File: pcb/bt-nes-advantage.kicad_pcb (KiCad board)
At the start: 2 copper layers, 78 x 35 mm, 20 parts, among them J1 USB_C_Receptacle_PowerOnly_6P, J2 Screw_Terminal_01x02, J3 Conn_01x08, U1 ESP32-C3_SUPERMINI_TH, U2 HW775

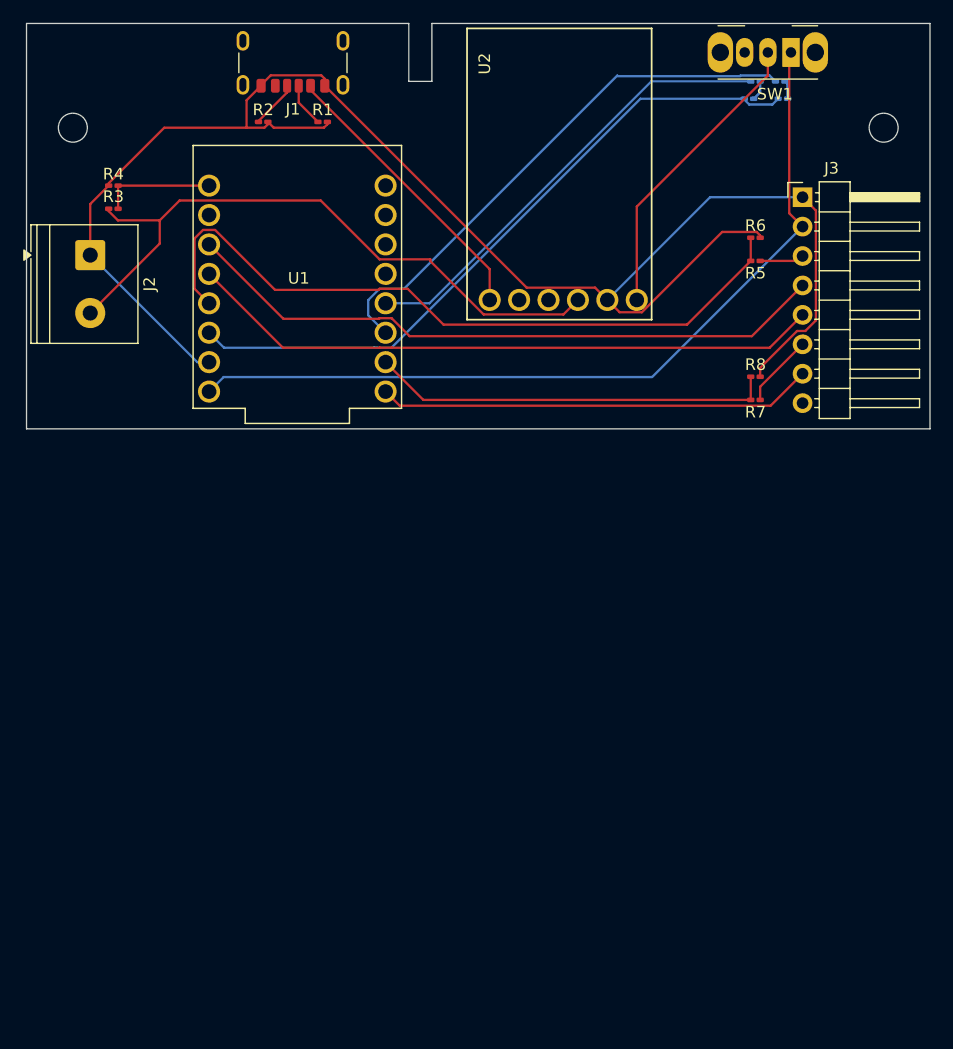
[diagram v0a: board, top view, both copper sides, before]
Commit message: New PCB revision. Updated firmware logic.
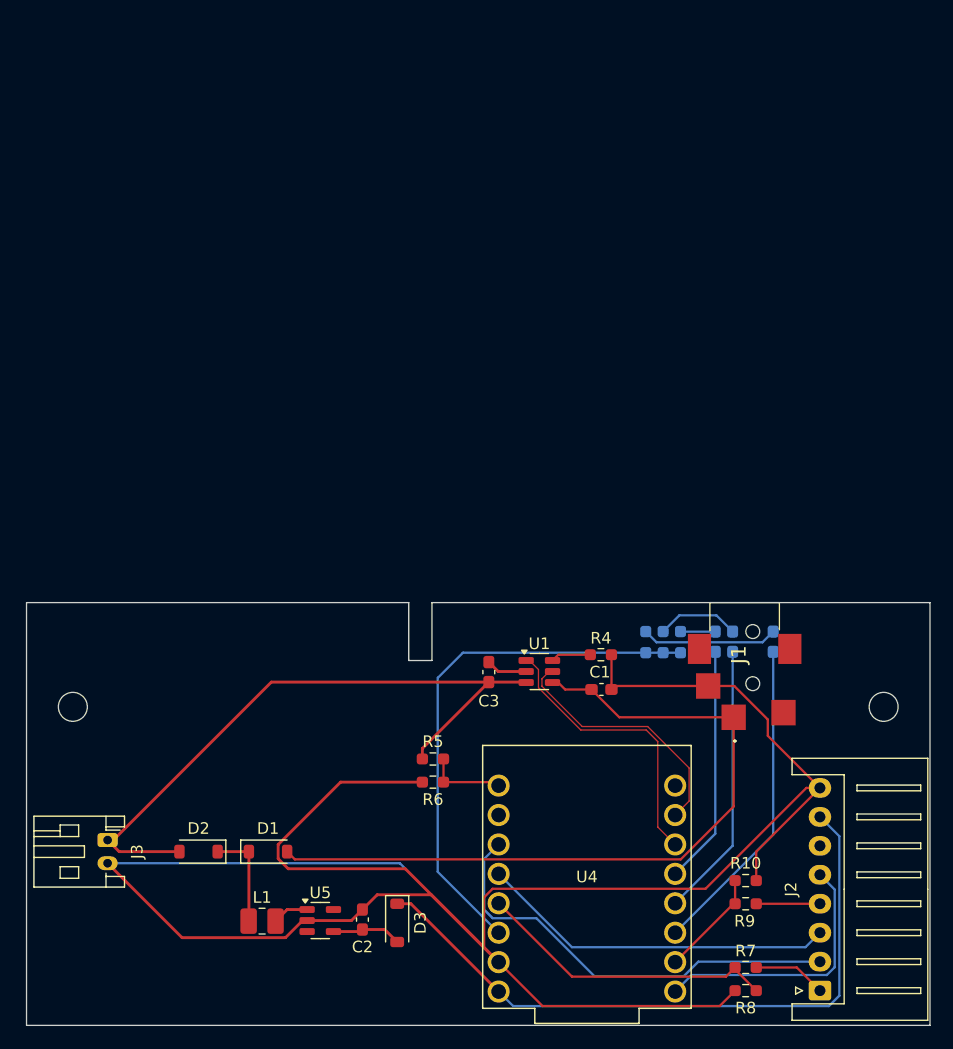
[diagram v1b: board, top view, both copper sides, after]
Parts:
- removed the REF** at (104.0, 59.0)
- removed the REF** at (174.0, 59.0)
- removed SW1: ~, Button_Switch_THT:SW_Slide_SPDT_Angled_CK_OS102011MA1Q
- removed U2: HW775, bt-nes-advantage:Charger2A
- added C1: 10µF, Capacitor_SMD:C_0603_1608Metric_Pad1.08x0.95mm_HandSolder, F.Cu at (149.6, 107.5)
- added C2: 22µF, Capacitor_SMD:C_0603_1608Metric_Pad1.08x0.95mm_HandSolder, F.Cu at (129.0, 127.4)
- added C3: 10µF, Capacitor_SMD:C_0603_1608Metric_Pad1.08x0.95mm_HandSolder, F.Cu at (139.9, 106.0)
- added D3: 1N5817W, Diode_SMD:D_SOD-123, F.Cu at (132.0, 127.7)
- added D4: LED, LED_SMD:LED_0603_1608Metric_Pad1.05x0.95mm_HandSolder, B.Cu at (164.5, 103.4)
- added D5: LED, LED_SMD:LED_0603_1608Metric_Pad1.05x0.95mm_HandSolder, B.Cu at (161.0, 103.4)
- added D6: LED, LED_SMD:LED_0603_1608Metric_Pad1.05x0.95mm_HandSolder, B.Cu at (159.5, 103.4)
- added L1: 2.2µH, Inductor_SMD:L_1008_2520Metric_Pad1.43x2.20mm_HandSolder, F.Cu at (120.3, 127.5)
- added REF**: MountingHole_2.5mm, MountingHole:MountingHole_2.5mm, F.Cu at (174.0, 109.0)
- added REF**: MountingHole_2.5mm, MountingHole:MountingHole_2.5mm, F.Cu at (104.0, 109.0)
- added U4: ESP32-C3_SUPERMINI_TH, My_Library:MODULE_ESP32-C3_SUPERMINI, F.Cu at (148.4, 123.7)
- added U5: TPS613222ADBV, Package_TO_SOT_SMD:SOT-23-5, F.Cu at (125.4, 127.5)
- D1, D2: value LED -> 1N5817W; footprint LED_SMD:LED_0201_0603Metric_Pad0.64x0.40mm_HandSolder -> Diode_SMD:D_SOD-123; moved to F.Cu
- J1: value USB_C_Receptacle_PowerOnly_6P -> PJ-043-SMT-TR; footprint Connector_USB:USB_C_Receptacle_GCT_USB4125-xx-x-0190_6P_TopMnt_Horizontal -> My_Library:PJ043SMTTR
- J2: value Screw_Terminal_01x02 -> Conn_01x08_Socket; footprint TerminalBlock_Phoenix:TerminalBlock_Phoenix_PT-1,5-2-5.0-H_1x02_P5.00mm_Horizontal -> Connector_JST:JST_XH_S8B-XH-A_1x08_P2.50mm_Horizontal
- J3: value Conn_01x08 -> 3.7V Lithium Battery; footprint Connector_PinHeader_2.54mm:PinHeader_1x08_P2.54mm_Horizontal -> Connector_JST:JST_PH_S2B-PH-K_1x02_P2.00mm_Horizontal
- R1, R2: value 5.1K -> 200; footprint Resistor_SMD:R_0201_0603Metric_Pad0.64x0.40mm_HandSolder -> Resistor_SMD:R_0603_1608Metric_Pad0.98x0.95mm_HandSolder; moved to B.Cu
- R10, R9: value 200 -> 1K; footprint Resistor_SMD:R_0201_0603Metric_Pad0.64x0.40mm_HandSolder -> Resistor_SMD:R_0603_1608Metric_Pad0.98x0.95mm_HandSolder; moved to F.Cu
- R3: value 100K -> 200; footprint Resistor_SMD:R_0201_0603Metric_Pad0.64x0.40mm_HandSolder -> Resistor_SMD:R_0603_1608Metric_Pad0.98x0.95mm_HandSolder; moved to B.Cu
- R4: value 100K -> 2K; footprint Resistor_SMD:R_0201_0603Metric_Pad0.64x0.40mm_HandSolder -> Resistor_SMD:R_0603_1608Metric_Pad0.98x0.95mm_HandSolder
- R5: value 1K -> 100K; footprint Resistor_SMD:R_0201_0603Metric_Pad0.64x0.40mm_HandSolder -> Resistor_SMD:R_0603_1608Metric_Pad0.98x0.95mm_HandSolder
- R6: value 2K -> 100K; footprint Resistor_SMD:R_0201_0603Metric_Pad0.64x0.40mm_HandSolder -> Resistor_SMD:R_0603_1608Metric_Pad0.98x0.95mm_HandSolder
- R7: footprint Resistor_SMD:R_0201_0603Metric_Pad0.64x0.40mm_HandSolder -> Resistor_SMD:R_0603_1608Metric_Pad0.98x0.95mm_HandSolder
- R8: value 2K -> 1K; footprint Resistor_SMD:R_0201_0603Metric_Pad0.64x0.40mm_HandSolder -> Resistor_SMD:R_0603_1608Metric_Pad0.98x0.95mm_HandSolder
- U1: value ESP32-C3_SUPERMINI_TH -> TP4057; footprint bt-nes-advantage:MODULE_ESP32-C3_SUPERMINI -> Package_TO_SOT_SMD:TSOT-23-6
- moved J2 89.4 mm to (168.5, 133.5), turned to 90 degrees
- moved D2 83.3 mm to (114.8, 121.5), turned to 180 degrees
- moved J3 81.7 mm to (107.0, 120.5), turned to -90 degrees
- moved D1 78.7 mm to (120.8, 121.5)
- moved R9 69.5 mm to (162.1, 126.0), turned to 0 degrees
- moved R10 67.6 mm to (162.1, 124.0)
- moved J1 65.8 mm to (162.0, 105.2), turned to -90 degrees
- moved R3 61.6 mm to (156.5, 103.4), turned to -90 degrees
- moved R4 58.4 mm to (149.6, 104.5), turned to 0 degrees
- moved R2 56.7 mm to (155.0, 103.4), turned to -90 degrees
- moved R6 54.6 mm to (135.1, 115.5)
- moved R8 53.0 mm to (162.1, 133.5)
- moved R1 52.9 mm to (153.5, 103.4), turned to -90 degrees
- moved R5 51.2 mm to (135.1, 113.5)
- moved R7 49.0 mm to (162.1, 131.5), turned to 0 degrees
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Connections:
- D1 pad 1: /LED 1 -> Net-(D1-K)
- D1 pad 2: Net-(D1-A) -> VBUS_5V
- D2 pad 1: /LED 2 -> Net-(D1-K)
- D2 pad 2: Net-(D2-A) -> VBAT
- J2 pad 1: GND -> DATA_0_5V
- J2 pad 2: +BATT -> LATCH
- J3 pad 1: GND -> VBAT
- J3 pad 2: +5V -> GND
- R1 pad 1: Net-(J1-CC1) -> Net-(D4-A)
- R1 pad 2: GND -> VDD_3V
- R10 pad 1: Net-(D2-A) -> GND
- R10 pad 2: +3.3V -> DATA_1
- R2 pad 1: Net-(J1-CC2) -> Net-(D5-A)
- R2 pad 2: GND -> VDD_3V
- R3 pad 1: +BATT -> Net-(D6-A)
- R3 pad 2: /BATT READ -> VDD_3V
- R4 pad 1: /BATT READ -> Net-(U1-PROG)
- R5 pad 1: /DATA 0 5V -> BATT_READ
- R5 pad 2: /DATA 0 -> VBAT
- R6 pad 1: /DATA 0 -> GND
- R6 pad 2: GND -> BATT_READ
- R7 pad 1: /DATA 1 5V -> DATA_0
- R7 pad 2: /DATA 1 -> DATA_0_5V
- R8 pad 1: /DATA 1 -> GND
- R8 pad 2: GND -> DATA_0
- R9 pad 1: Net-(D1-A) -> DATA_1
- R9 pad 2: +3.3V -> DATA_1_5V
- U1 pad 1: unconnected-(U1-GPIO1-Pad1) -> BATT_CHRG
- U1 pad 2: /LATCH -> GND
- U1 pad 3: /CLOCK 0 -> VBAT
- U1 pad 4: /DATA 0 -> VBUS_5V
- U1 pad 5: /CLOCK 1 -> BATT_STDBY
- U1 pad 6: /DATA 1 -> Net-(U1-PROG)
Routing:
- net GND: track 141.3 -> 217.3 mm
- net +5V: track 72.7 -> 0.00 mm
- net VBUS_5V: track 0.00 -> 65.3 mm
- net /DATA 0: track 62.2 -> 0.00 mm
- net +3.3V: track 59.0 -> 0.00 mm
- net VDD_5V: track 0.00 -> 58.3 mm
- net VBAT: track 0.00 -> 57.4 mm
- net +BATT: track 56.9 -> 0.00 mm
- net /LATCH: track 56.4 -> 0.00 mm
- net /CLOCK 0: track 55.1 -> 0.00 mm
- net /LED 2: track 46.9 -> 0.00 mm
- net VDD_3V: track 0.00 -> 46.0 mm
- net /LED 1: track 39.5 -> 0.00 mm
- net LATCH: track 0.00 -> 38.1 mm
- net /CLOCK 1: track 37.6 -> 0.00 mm
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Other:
- board size 78 x 35 mm -> 78 x 36.5 mm

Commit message: pcb update
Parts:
- J1: footprint My_Library:PJ043SMTTR -> My_Library:CUI_PJ-040-SMT-TR
- moved D5 3.20 mm to (164.0, 102.4)
- moved D6 3.20 mm to (162.5, 102.4)
- moved R1 3.20 mm to (156.5, 102.4)
- moved R2 3.20 mm to (158.0, 102.4)
- moved R3 3.20 mm to (159.5, 102.4)
- moved J1 2.83 mm to (164.0, 103.2), turned to 180 degrees
- moved D4 1.44 mm to (165.5, 102.4)
- turned C3 to -90 degrees
- renumbered U5 to U2, U4 to U3
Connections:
- J1 pad 3: unconnected-(J1-Pad3) -> GND
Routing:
- net GND: track 217.3 -> 229.8 mm
- net VBAT: track 57.4 -> 45.6 mm
- net VBUS_5V: track 65.3 -> 70.1 mm
- net VDD_3V: track 46.0 -> 41.3 mm
- net LED3: track 20.6 -> 22.9 mm
- net LED2: track 23.8 -> 26.0 mm
- net Net-(D4-A): track 11.8 -> 9.81 mm
- net LED1: track 27.8 -> 29.2 mm
- net BATT_STDBY: track 22.0 -> 21.0 mm

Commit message: Added silkscreen labels for the LED indicators.
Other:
- board text added: "BLUE"
- board text added: "GREEN"
- board text added: "RED"
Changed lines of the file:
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@@
+		(layer "B.SilkS")
+	)
+	(gr_line
+		(start 167 102)
+		(end 167 101.5)
+		(stroke
+			(width 0.1)
+			(type default)
+		)
 		(layer "B.SilkS")
 	)
@@
 		(layer "B.SilkS")
 	)
+	(gr_line
+		(start 167 103.5)
+		(end 167 103)
+		(stroke
+			(width 0.1)
+			(type default)
+		)
+		(layer "B.SilkS")
+	)
 	(gr_poly
 		(pts
@@
 		)
 		(fill yes)
+		(layer "B.SilkS")
+	)
+	(gr_line
+		(start 166.5 103)
+		(end 167 103)
+		(stroke
+			(width 0.1)
+			(type default)
+		)
+		(layer "B.SilkS")
+	)
+	(gr_line
+		(start 167.5 103)
+		(end 167 103)
+		(stroke
+			(width 0.1)
+			(type default)
+		)
 		(layer "B.SilkS")
 	)
@@
 	(gr_poly
 		(pts
+			(xy 166.5 102) (xy 167.5 102) (xy 167 103)
+		)
+		(stroke
+			(width 0.1)
+			(type solid)
+		)
+		(fill yes)
+		(layer "B.SilkS")
+	)
+	(gr_poly
+		(pts
 			(xy 134.798211 110.895425) (xy 134.820099 110.894367) (xy 134.842048 110.893743) (xy 134.864038 110.893479)
 			(xy 134.886048 110.893503) (xy 134.930048 110.894115) (xy 134.973886 110.894992) (xy 134.975749 110.499147)
@@
 		(layer "Edge.Cuts")
 	)
+	(gr_text "RED"
+		(at 166.235 106.5 90)
+		(layer "B.SilkS")
+		(effects
+			(font
+				(size 1 1)
+				(thickness 0.15)
+			)
+			(justify left bottom mirror)
+		)
+	)
 	(gr_text "Bluetooth NES Advantage 1.0"
 		(at 146 110 0)
@@
 		)
 	)
+	(gr_text "GREEN"
+		(at 163 106.5 90)
+		(layer "B.SilkS")
+		(effects
+			(font
+				(size 1 1)
+				(thickness 0.15)
+			)
+			(justify left bottom mirror)
+		)
+	)
+	(gr_text "BLUE"
+		(at 164.5 109.5 90)
+		(layer "B.SilkS")
+		(effects
+			(font
+				(size 1 1)
+				(thickness 0.15)
+			)
+			(justify left bottom mirror)
+		)
+	)
